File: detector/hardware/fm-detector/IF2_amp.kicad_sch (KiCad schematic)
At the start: 11 parts, among them J3 U.FL, Q3 BSS138

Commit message: pulse detector design
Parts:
- removed C11: 4.7n, g-cap:C_0603_1608Metric, symbol #gplm:cap/CAP-0000-0472
- removed C12, C13, C14: 1.5n, g-cap:C_0603_1608Metric, symbol #gplm:cap/CAP-0000-0152
- removed C26: 100n, g-cap:C_0603_1608Metric, symbol #gplm:cap/CAP-0000-0104
- removed J3: U.FL, g-con:U.FL_Hirose_U.FL-R-SMT-1_Vertical, symbol #gplm:con/CON-0001-0000
- removed L4: 3µ9, g-ind:L_Coilcraft_1008HQ_2520Metric, symbol #gplm:ind/IND-0002-0392
- removed L5: 8µ2, g-ind:L_Coilcraft_1008HQ_2520Metric, symbol #gplm:ind/IND-0002-0822
- removed L6: 2µ7, g-ind:L_Coilcraft_1008HQ_2520Metric, symbol #gplm:ind/IND-0002-0272
- removed Q3: BSS138, g-SOT:SOT-23-3, symbol #gplm:trs/TRS-0001-0000
- removed RV1: 10K, g-rvr:Potentiometer_Bourns_3314J_Vertical, symbol #gplm:rvr/RVR-0000-1002
- added C1, C2, C24, C3, C5: 100n, g-cap:C_0603_1608Metric, symbol #gplm:cap/CAP-0000-0104
- added C4: 4.7n, g-cap:C_0603_1608Metric, symbol #gplm:cap/CAP-0000-0472
- added C6: 12n, g-cap:C_0603_1608Metric, symbol #gplm:cap/CAP-0000-0123
- added J5, J7: U.FL, g-con:U.FL_Hirose_U.FL-R-SMT-1_Vertical, symbol #gplm:con/CON-0001-0000
- added L2, L3: 18µ, g-ind:L_Murata_LQW32FT_3225, symbol #gplm:ind/IND-0003-0183
- added Q1: MMBT3904, g-SOT:SOT-23-3, symbol #gplm:trs/TRS-0000-0001
- added R1: 51E, g-res:R_0603_1608Metric, symbol #gplm:res/RES-0000-0510
- added R2: 3K6, g-res:R_0603_1608Metric, symbol #gplm:res/RES-0000-3601
- added R3: 1K5, g-res:R_0603_1608Metric, symbol #gplm:res/RES-0000-1501
- added R4: 1K2, g-res:R_0603_1608Metric, symbol #gplm:res/RES-0000-1201
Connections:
- net +5V: now also C5.2, Q1.3 (C), R2.2
- net GND: now also C4.1, C5.1, C6.1, J5.2 (Ext), J7.2 (Ext), R1.1, R3.1, R4.1
- new net: C3.1, Q1.2 (E), R4.2
- new net: C3.2, C4.2, L2.1
- new net: C1.2, C2.2, Q1.1 (B), R2.1, R3.2
- new net: C1.1, R1.2
- new net: L2.2, L3.1
- new net IF2_amp_stage/IN: C6.2, L3.2
- new net IF2_amp_stage2/OUT: C24.1
- new net IN: C2.1, J7.1 (In)
- new net OUT: C24.2, J5.1 (In)
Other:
- added sheet IF2_amp_stage (IF2_amp_sub.kicad_sch)
- added sheet IF2_amp_stage1 (IF2_amp_sub.kicad_sch)
- added sheet IF2_amp_stage2 (IF2_amp_sub.kicad_sch)
- title: IF2 Mixer -> Low frequency amplifier (< 200 kHz)

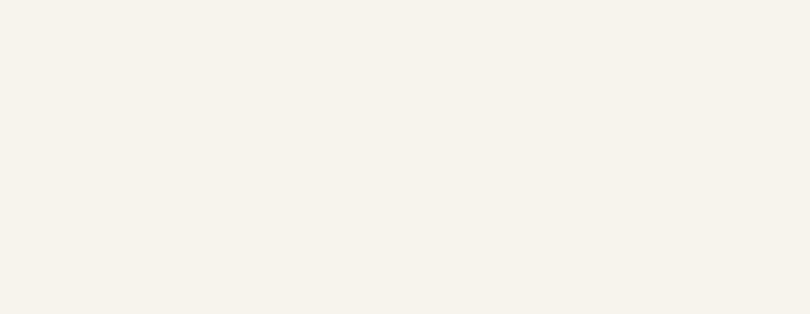
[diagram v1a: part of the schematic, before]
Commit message: Schematic for PCB-0010-0100
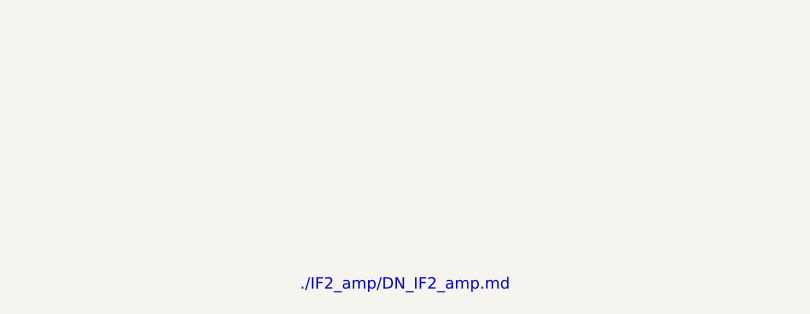
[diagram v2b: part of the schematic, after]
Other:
- note added: "./IF2_amp/DN_IF2_amp.md"
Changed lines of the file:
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@@
 		(title "Low frequency amplifier (< 200 kHz)")
+	)
+	(text "./IF2_amp/DN_IF2_amp.md"
+		(exclude_from_sim no)
+		(at 115.57 129.54 0)
+		(effects
+			(font
+				(size 1.27 1.27)
+			)
+			(href "https://github.com/LieBtrau/MegawattKS_Radio_Design_101/blob/main/IF2_amp/DN_IF2_amp.md")
+		)
 	)
 	(junction
